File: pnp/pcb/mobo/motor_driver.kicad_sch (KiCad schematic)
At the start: 24 parts, among them M9 Stepper_Motor, U5 TMC2226

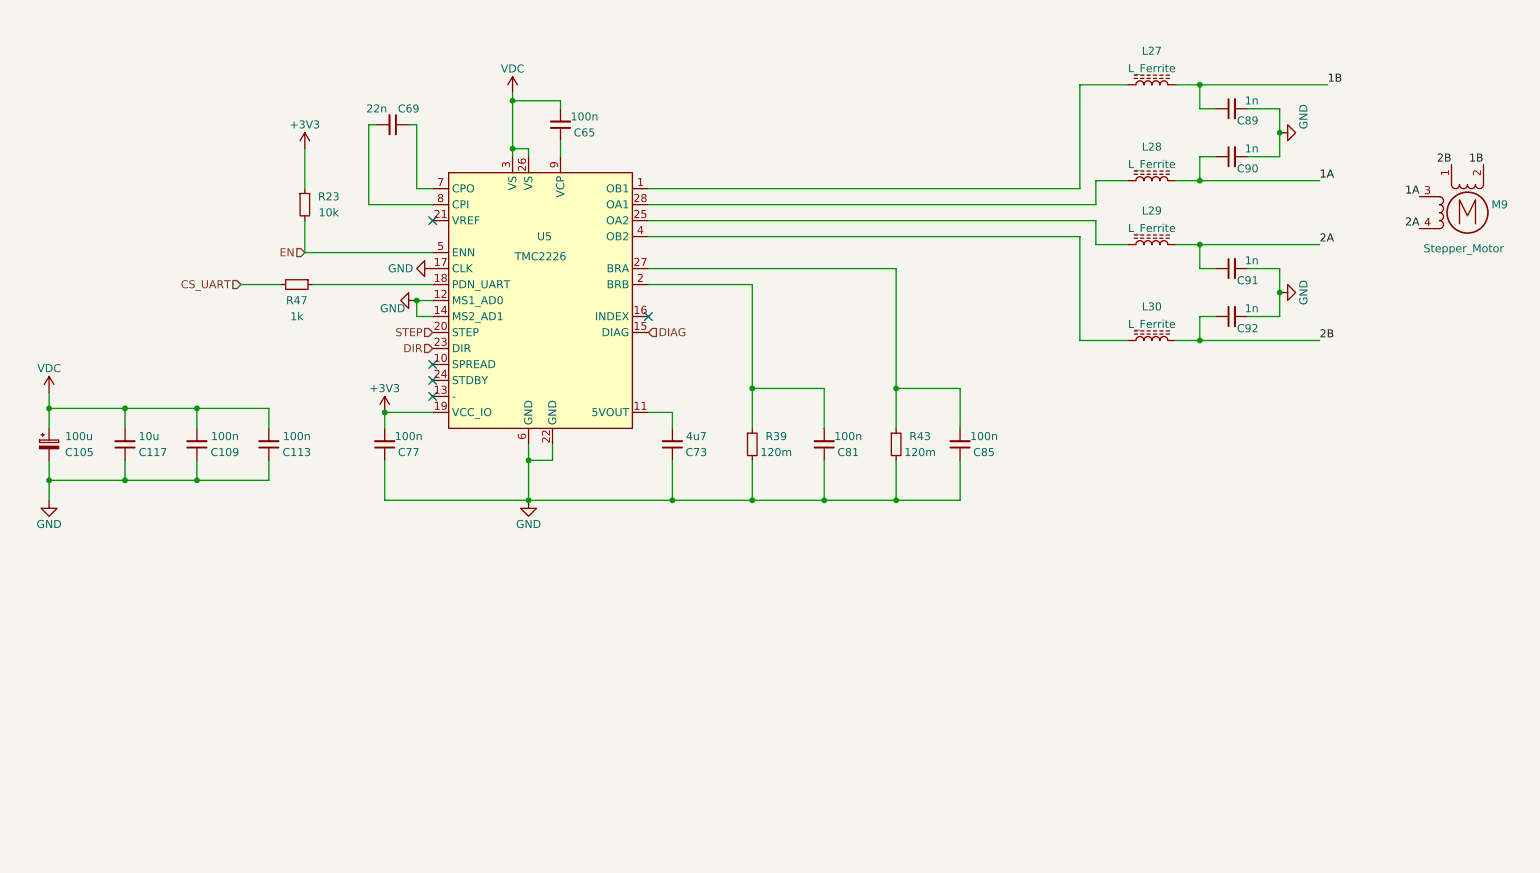
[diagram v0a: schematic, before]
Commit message: Motor driver new Symbol and fix TVS placement
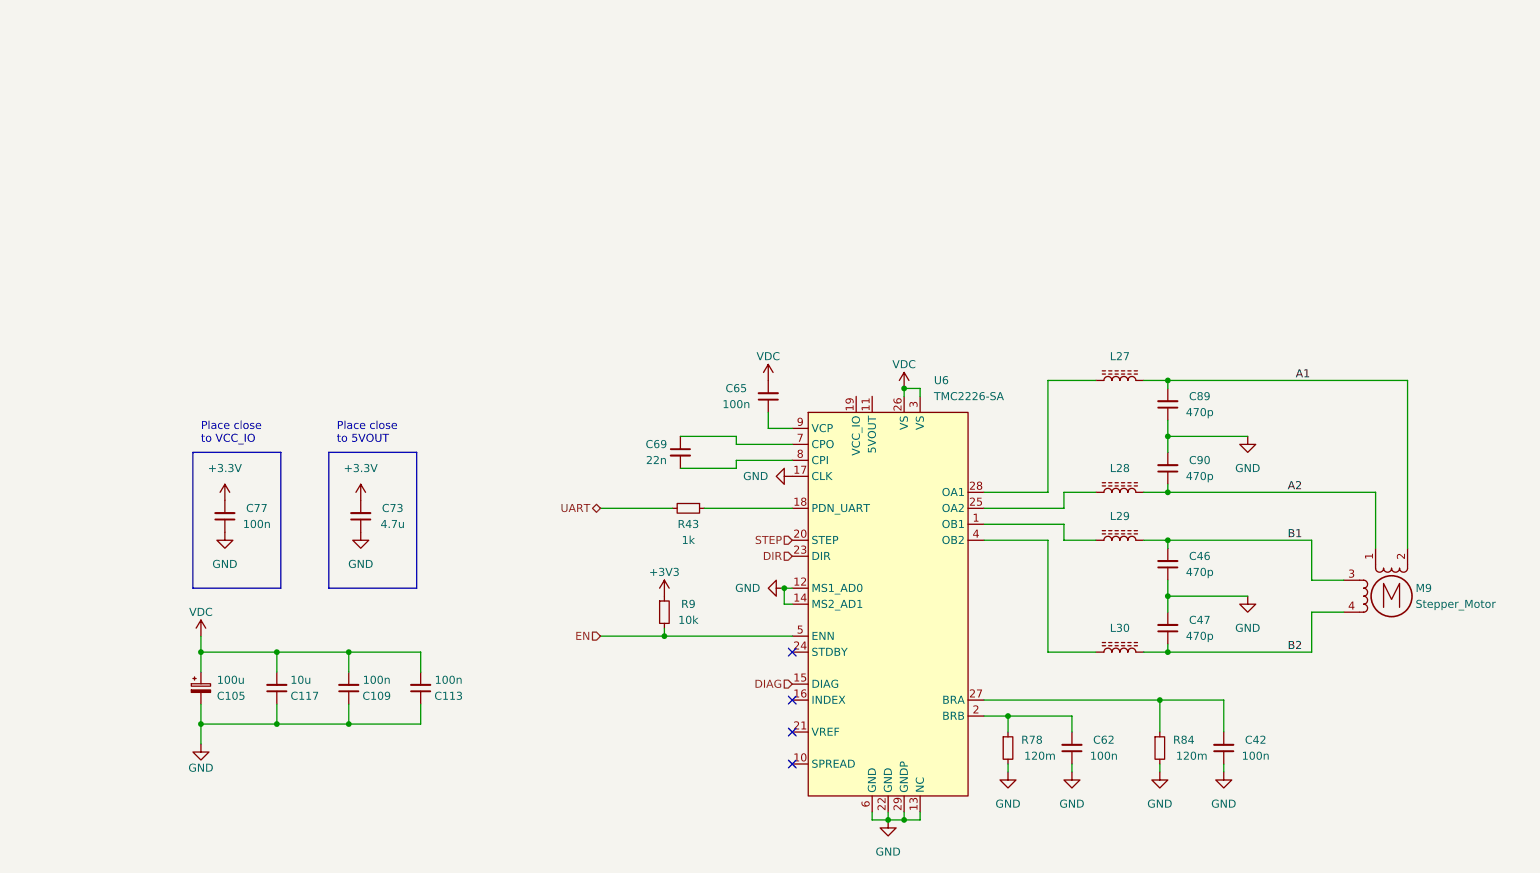
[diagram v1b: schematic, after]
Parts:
- removed C81, C85: 100n, Capacitor_SMD:C_0805_2012Metric, symbol Device:C_Small
- removed C91, C92: 1n, Capacitor_SMD:C_0805_2012Metric, symbol Device:C_Small
- removed R23: 10k, Resistor_SMD:R_0805_2012Metric, symbol Device:R_Small
- removed R39: 120m, Resistor_SMD:R_0805_2012Metric, symbol Device:R_Small
- removed R47: 1k, Resistor_SMD:R_0805_2012Metric, symbol Device:R_Small
- removed U5: TMC2226, Package_SO:HTSSOP-28-1EP_4.4x9.7mm_P0.65mm_EP2.85x5.4mm_ThermalVias, symbol index:TMC2226
- added C42, C62: 100n, Capacitor_SMD:C_0805_2012Metric, symbol Device:C_Small
- added C46, C47: 470p, Capacitor_SMD:C_0805_2012Metric, symbol Device:C_Small
- added R78, R84: 120m, Resistor_SMD:R_1206_3216Metric, symbol Device:R_Small
- added R9: 10k, Resistor_SMD:R_0805_2012Metric, symbol Device:R_Small
- added U6: TMC2226-SA, Package_SO:HTSSOP-28-1EP_4.4x9.7mm_P0.65mm_EP2.75x6.2mm_ThermalVias, symbol index:TMC2226-SA
- C69: Notes 50V/10% -> 50V
- C73: value 4u7 -> 4.7u
- C89, C90: value 1n -> 470p; Notes 50V/10% -> 100V
- L27, L28, L29, L30: footprint index:L_0805_2012Metric -> Inductor_SMD:L_0805_2012Metric; Notes 120R @ 100MHz/6A -> 150R @ 100MHz
- R43: value 120m -> 1k
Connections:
- net +3V3: now also R9.1; no longer C77.2
- net DIAG: now also U6.15 (DIAG)
- net DIR: now also U6.23 (DIR)
- net EN: now also R9.2, U6.5 (ENN)
- net GND: now also C89.1, C42.1, C46.1, C47.2, C62.1, R78.2, R84.2, U6.12 (MS1_AD0), U6.13 (NC), U6.14 (MS2_AD1), U6.17 (CLK), U6.22 (GND), U6.29 (GNDP), U6.6 (GND); no longer C89.2, R43.2
- net STEP: now also U6.20 (STEP)
- net VDC: now also U6.26 (VS), U6.3 (VS)
- net at R43.1: now also U6.18 (PDN_UART)
- net at C69.1: now also U6.7 (CPO)
- net at C69.2: now also U6.8 (CPI)
- net at L28.1: now also U6.25 (OA2)
- net at L30.1: now also U6.4 (OB2)
- net at L27.1: now also U6.28 (OA1)
- net +3.3V: now reaches C73.2
- net +3.3V: now also C77.2
- net at L29.1: now also U6.1 (OB1)
- net at C65.1: now also U6.9 (VCP)
- net 1A renamed A2
- net A2: now also M9.1; no longer M9.3
- net 1B renamed A1
- net A1: now also C89.2; no longer C89.1
- net 2A renamed B1
- net B1: now also M9.3, C46.2; no longer M9.4
- net 2B renamed B2
- net B2: now also M9.4, C47.1; no longer M9.1
- new net: C42.2, R84.1, U6.27 (BRA)
- new net: C62.2, R78.1, U6.2 (BRB)
- new net UART: R43.2
- no-connect marks 5 -> 4
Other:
- note added: "Place close to 5VOUT"
- note added: "Place close to VCC_IO"
- moved on the sheet: C105, C109, C113, C117, C65, C69, C73, C77, C89, C90, L27, L28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

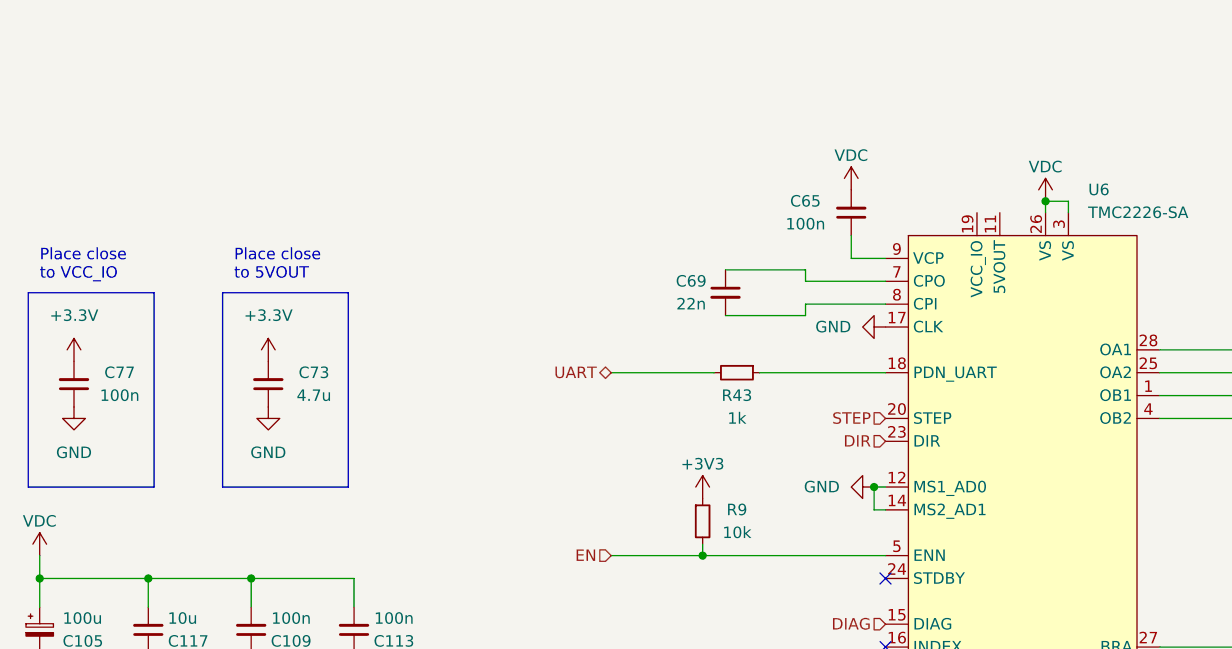
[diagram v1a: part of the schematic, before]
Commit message: Increased motor driver sense resistor package size
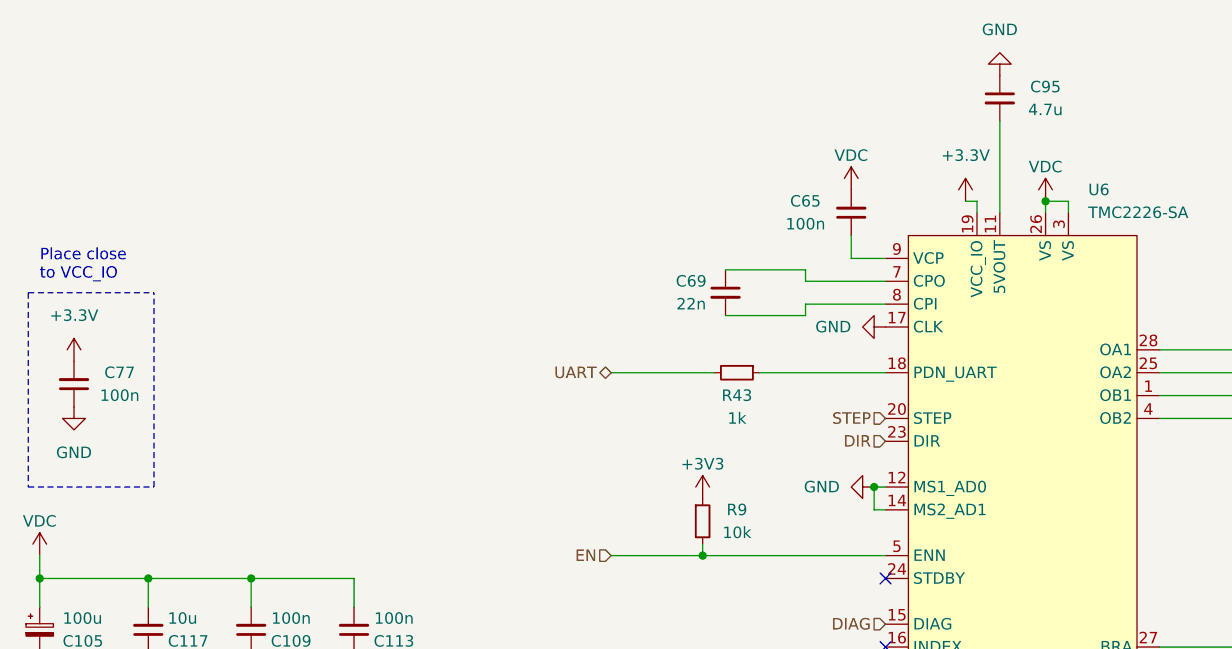
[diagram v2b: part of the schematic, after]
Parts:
- removed C73: 4.7u, Capacitor_SMD:C_0805_2012Metric, symbol Device:C_Small
- added C95: 4.7u, Capacitor_SMD:C_0805_2012Metric, symbol Device:C_Small
- R78, R84: footprint Resistor_SMD:R_1206_3216Metric -> Resistor_SMD:R_1210_3225Metric; JLCPCB C17513 -> C620635; LCSC C17513 -> C620635; Notes 125mW/1% -> 0.5W
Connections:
- net +3.3V: now also U6.19 (VCC_IO)
- net GND: now also C95.1
- net at U6.11 (5VOUT): now also C95.2
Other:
- note removed: "Place close to 5VOUT"

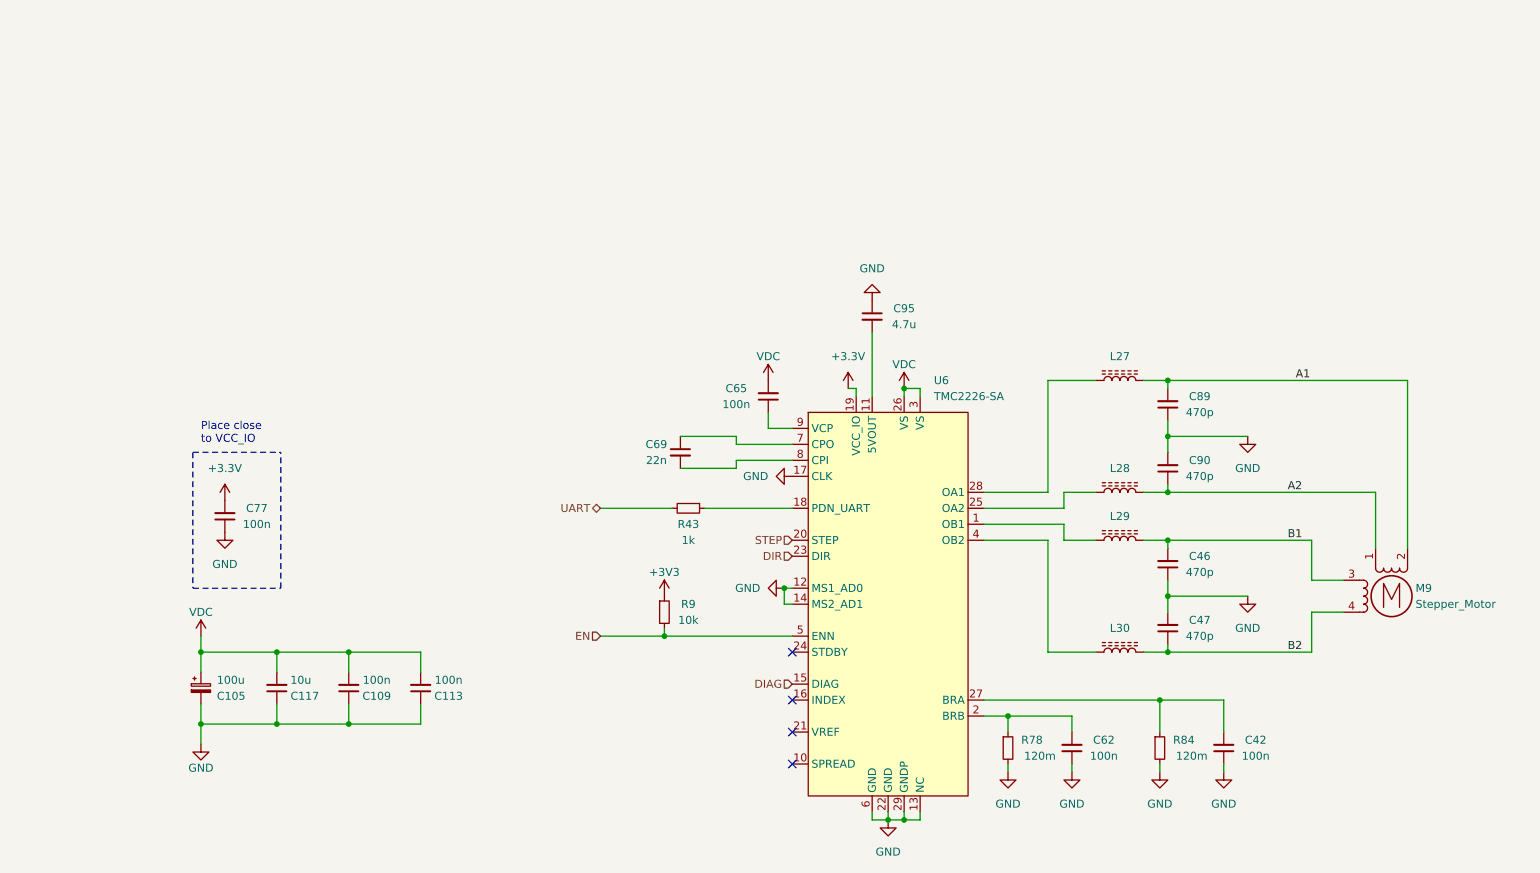
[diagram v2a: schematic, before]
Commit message: Add link to check symbol approval status
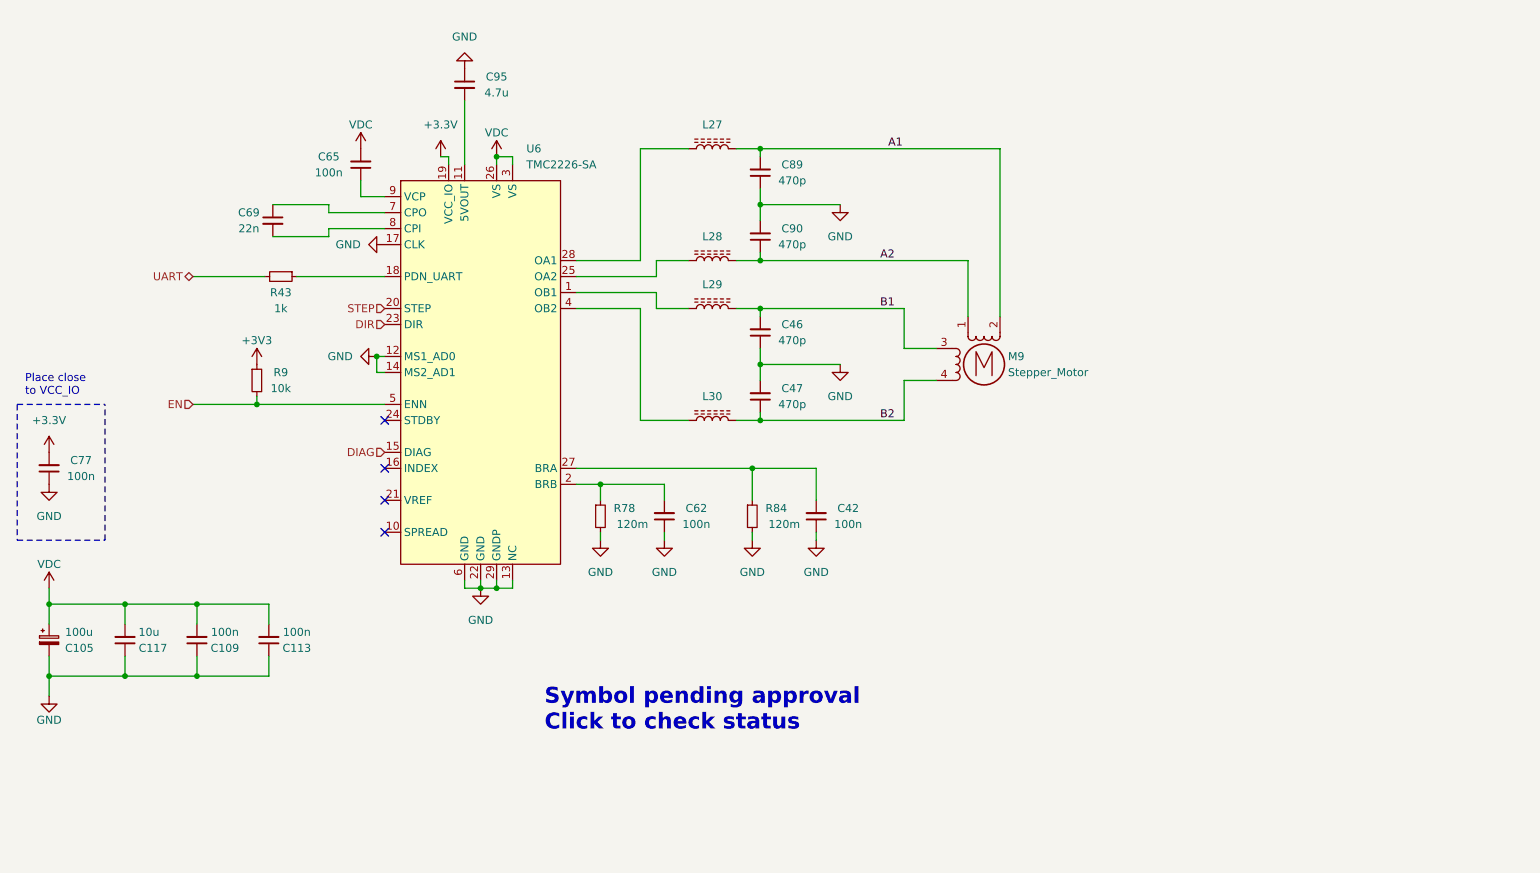
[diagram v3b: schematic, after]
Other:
- note added: "Symbol pending approval Click to check status"
- moved on the sheet: C105, C109, C113, C117, C42, C46, C47, C62, C65, C69, C77, C89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

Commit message: Removed Servos and added test points
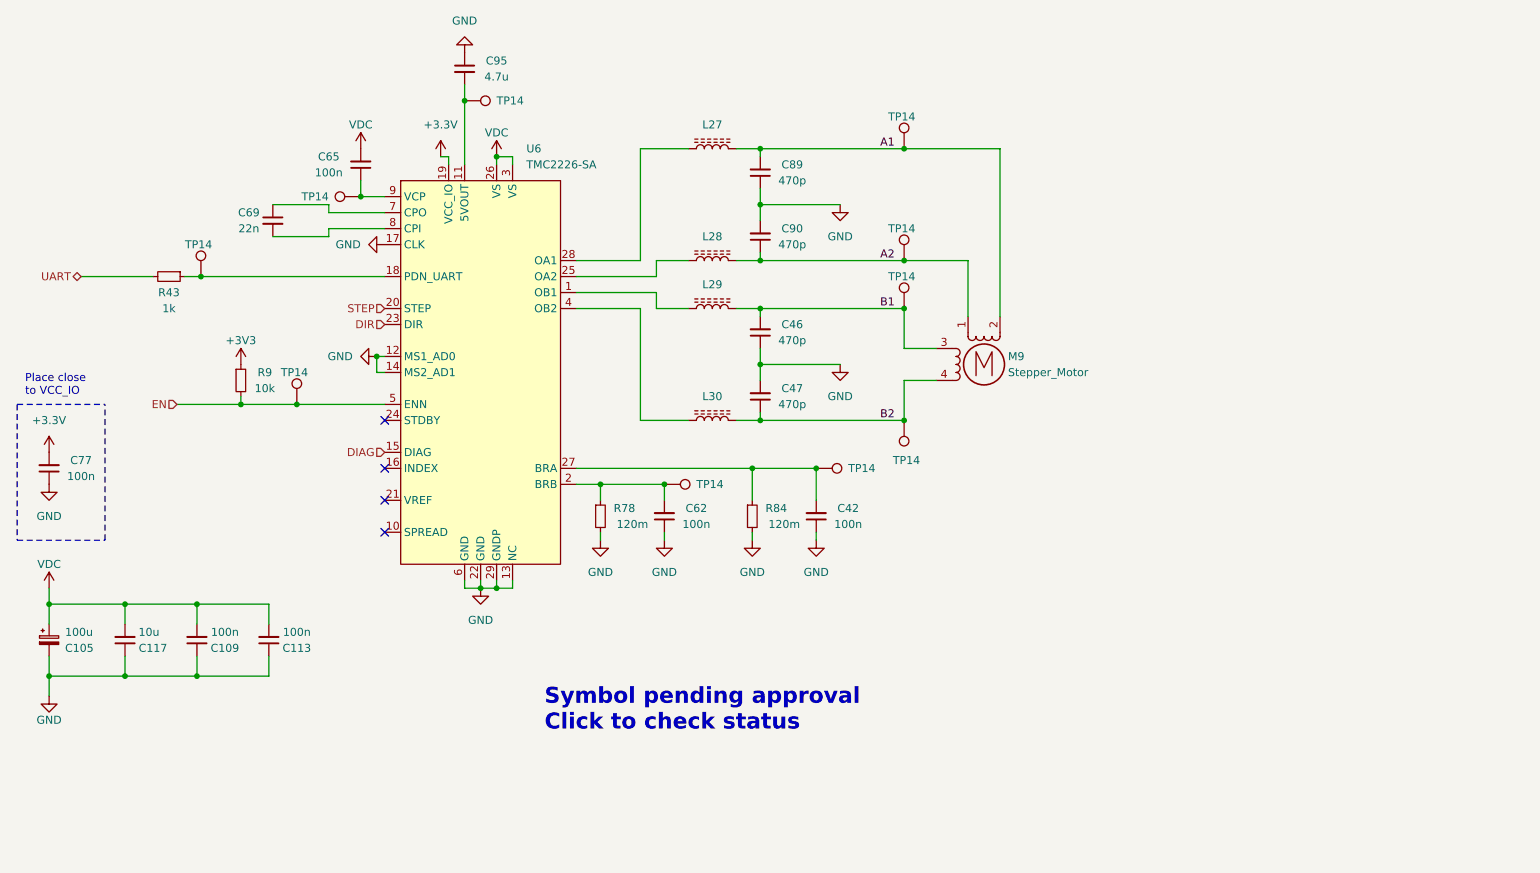
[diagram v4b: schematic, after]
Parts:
- added TP14 (x10): BOOT0_TestPoint, TestPoint:TestPoint_Pad_D2.0mm, symbol Connector:TestPoint
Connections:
- net A1: now also TP14.1
- net A2: now also TP14.1
- net B1: now also TP14.1
- net B2: now also TP14.1
- net EN: now also TP14.1
- net at C95.2, U6.11 (5VOUT): now also TP14.1
- net at C42.2, R84.1, U6.27 (BRA): now also TP14.1
- net at R43.1, U6.18 (PDN_UART): now also TP14.1
- net at C65.1, U6.9 (VCP): now also TP14.1
- net at C62.2, R78.1, U6.2 (BRB): now also TP14.1
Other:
- moved on the sheet: C95, R43, R9

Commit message: Mobo parts sourced
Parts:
- C105: JLCPCB C99837 -> C3339; Notes 35V/20%/Aluminum -> 35V/Aluminum
- C109, C113, C65: Digikey 1276-1020-1-ND -> (none); JLCPCB (none) -> C49678; LCSC (none) -> C476766; Notes 50V/10% -> 50V
- C117: JLCPCB (none) -> C440198; LCSC (none) -> C440198; Notes 50V/10% -> 50V
- C42, C62, C77: Digikey 1276-1020-1-ND -> (none); JLCPCB (none) -> C49678; LCSC (none) -> C476766; Notes 50V/10% -> 6.3V
- C46, C47, C89, C90: JLCPCB (none) -> C513677; LCSC (none) -> C513677
- C69: JLCPCB (none) -> C1729; LCSC (none) -> C107147; Notes 50V -> 10V
- C95: JLCPCB (none) -> C1779; LCSC (none) -> C1779; Notes 50V/10% -> 6.3V
- L27, L28, L29, L30: JLCPCB (none) -> C1015; LCSC (none) -> C1015; Notes 150R @ 100MHz -> 50R @ 100MHz
- M9: JLCPCB C37815 -> C2845453; LCSC C37815 -> C2845453
- R43: Notes 125mW/1% -> (none)
- R9: JLCPCB C17513 -> C17414; LCSC C17513 -> C17414; Notes 125mW/1% -> (none)
- TP14: value BOOT0_TestPoint -> TestPoint
- U6: JLCPCB (none) -> C705366; LCSC (none) -> C705366
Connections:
- net +3V3 is gone; now on net +3.3V: R9.1
- net 5VOUT: now reaches C95.2, TP14.1, U6.11 (5VOUT)
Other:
- moved on the sheet: C95, TP14
